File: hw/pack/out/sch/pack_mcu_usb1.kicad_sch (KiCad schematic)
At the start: 23 parts, among them J2 USB-C, J3 SWD, U1 BT40NE, U7 USBLC6-2SC6

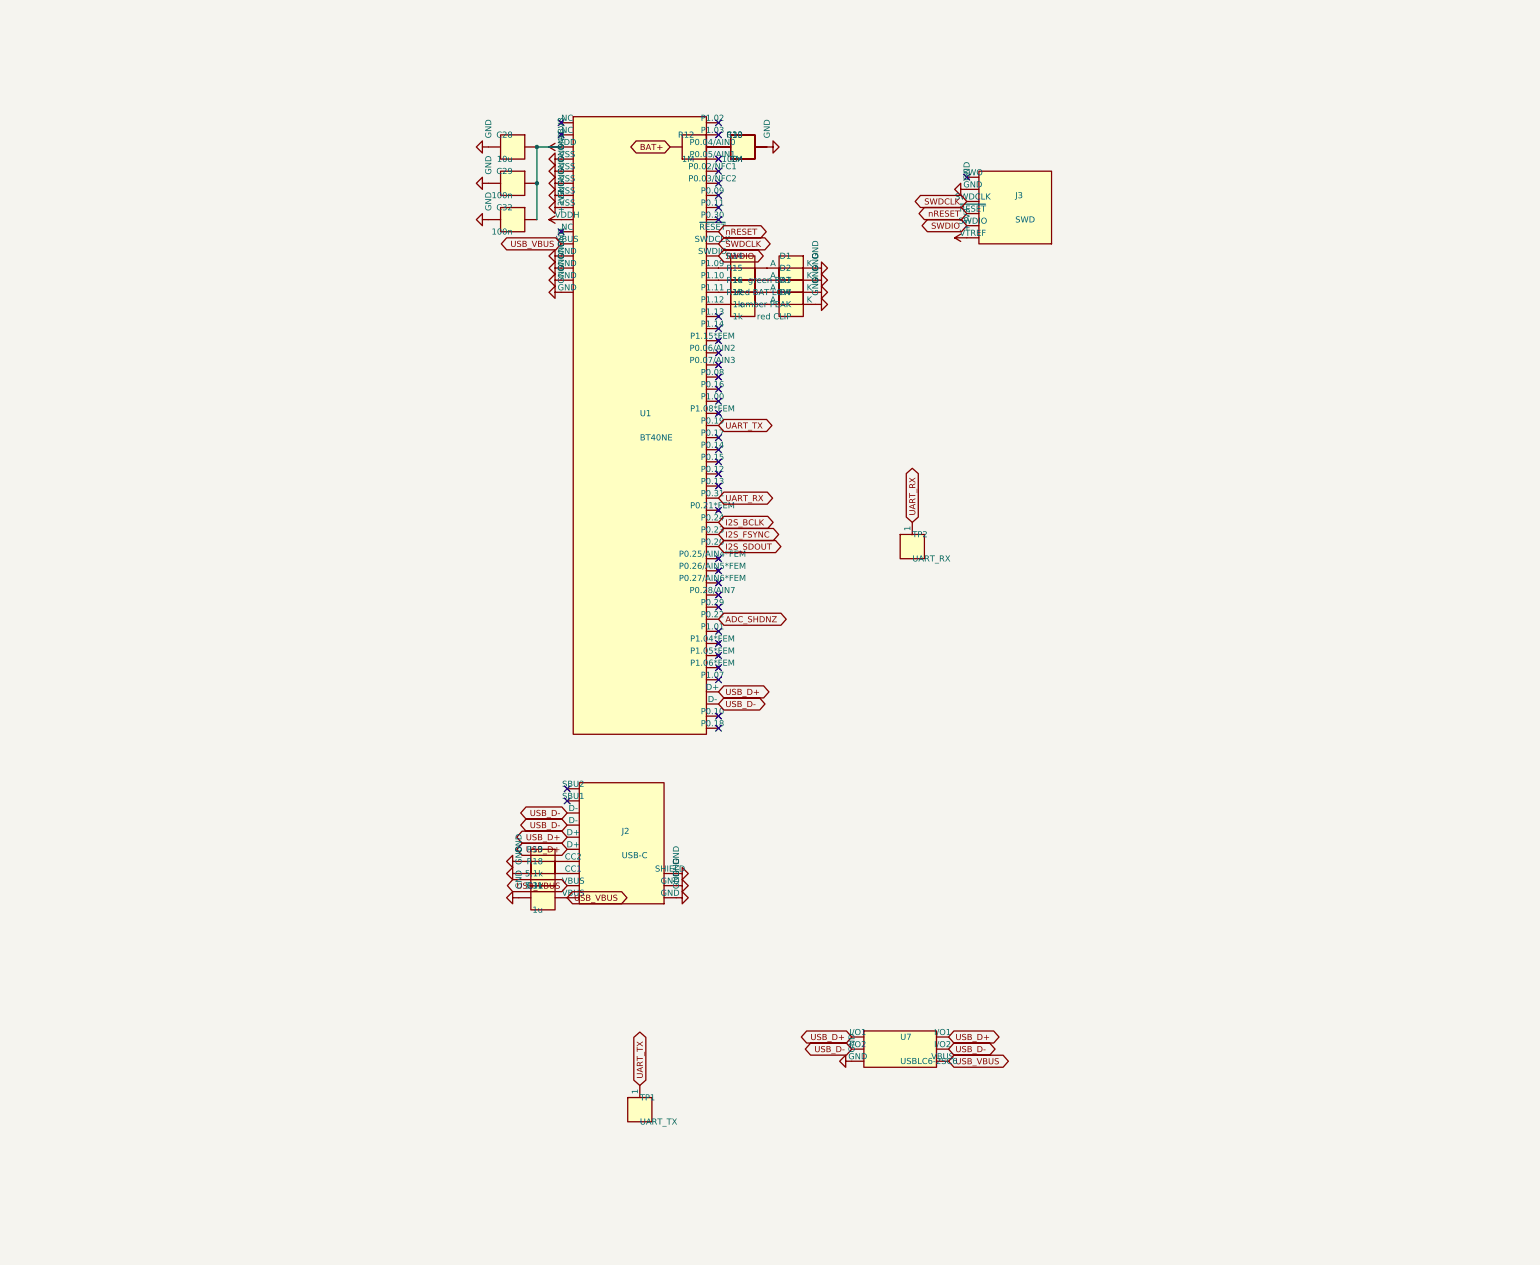
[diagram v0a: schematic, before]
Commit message: pack: #104 review fixes: 1 mm L1 battery path, test points, clip inserts off the antenna, pigtail route, JLC LCSC/rotations (#34)
- router: 'bat' class (1.0 mm, L1 only, necks <=1.36 mm at small pads);
  SW1 on-throw moved to pin 3 so feed and VSYS don't cross; 40 mOhm path
- audit.py: cell path from the board tracks (121 mOhm total, est. spring):
  cutoff computes 3.2012 V -> rounds to 3.3 V (reported, not tuned)
- TP3-TP11 folded in from review-104-tps (415194b), TP5/TP9-11 moved
- mech: clip inserts to (-24,3)/(-24,17) under the board; PIGTAIL route,
  bend radius, tie-down; fit.py checks both
- outputs: LCSC # per BOM line (verified), DNP/CONSIGN, CPL rotation table
- tests: battery path layer/width/R, BOM LCSC-or-DNP, rotation table

Co-Authored-By: Claude Opus 5.5 <noreply@anthropic.com>
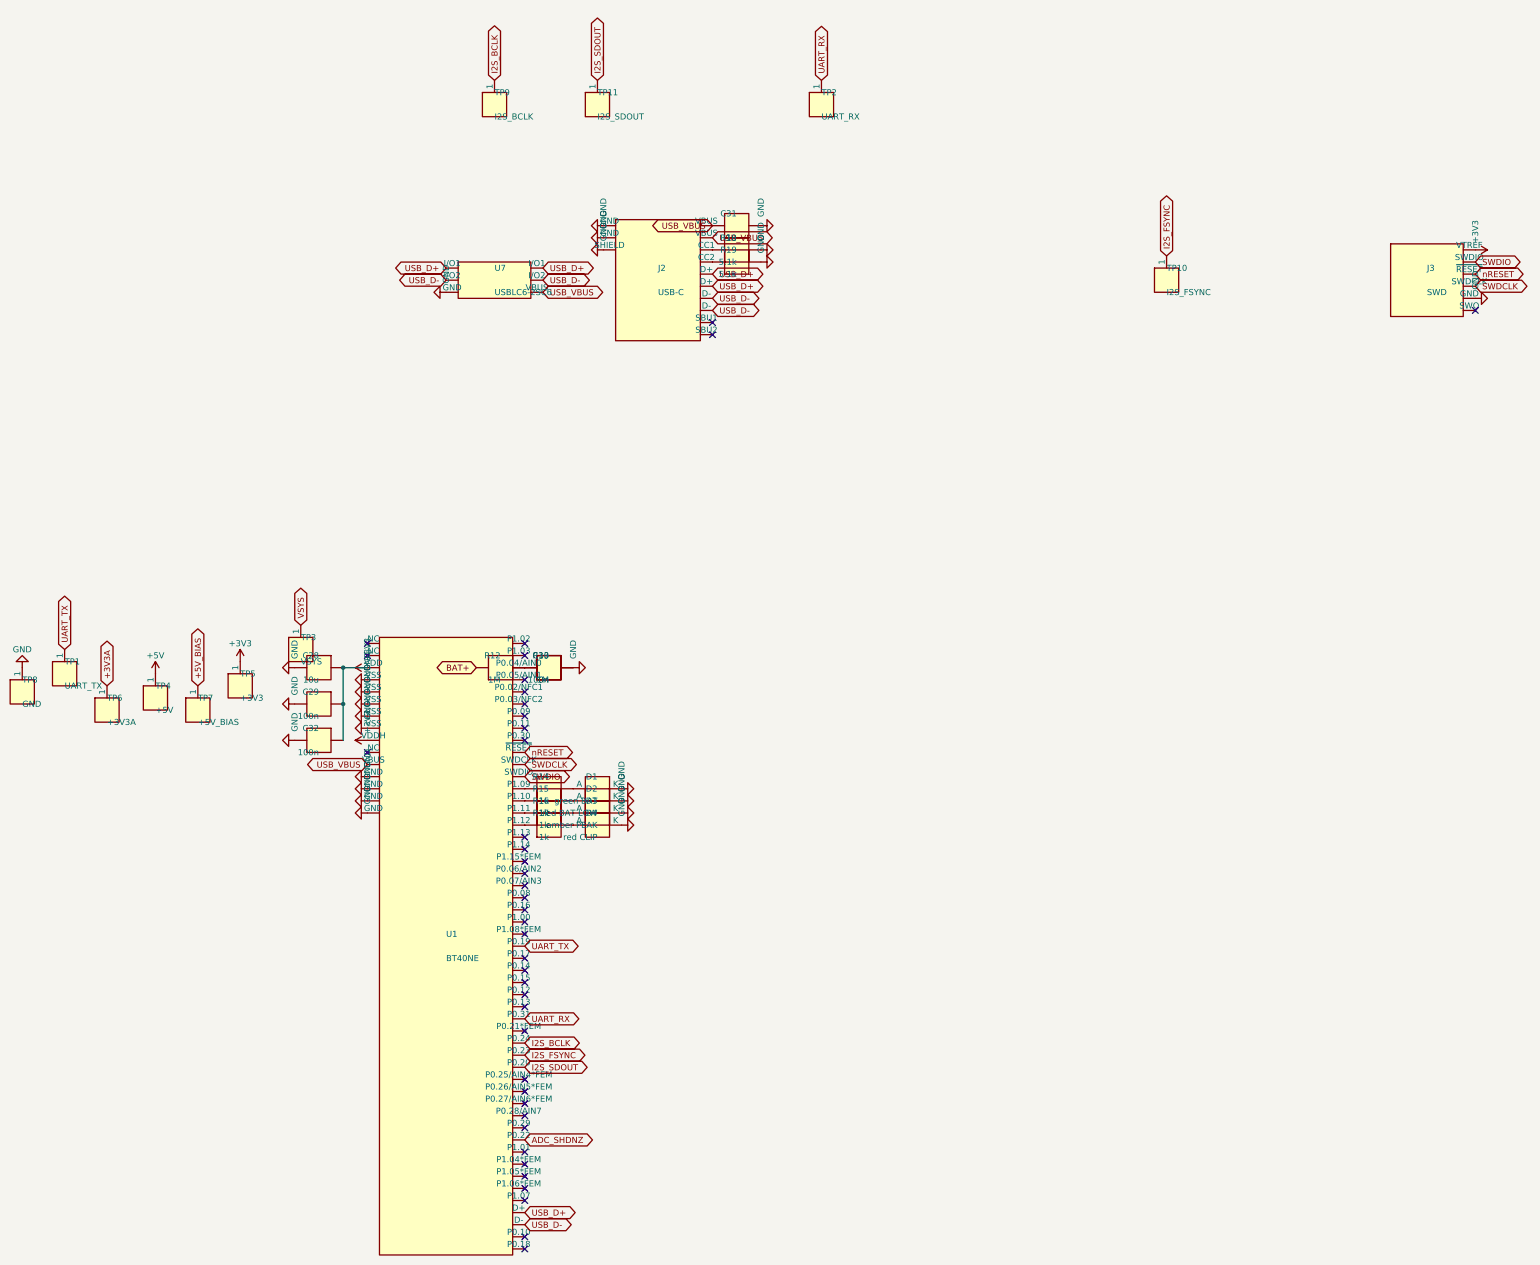
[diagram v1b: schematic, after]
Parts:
- added TP10: I2S_FSYNC, TestPoint:TestPoint_Pad_D1.0mm, symbol openpack:TestPoint
- added TP11: I2S_SDOUT, TestPoint:TestPoint_Pad_D1.0mm, symbol openpack:TestPoint
- added TP3: VSYS, TestPoint:TestPoint_Pad_D1.0mm, symbol openpack:TestPoint
- added TP4: +5V, TestPoint:TestPoint_Pad_D1.0mm, symbol openpack:TestPoint
- added TP5: +3V3, TestPoint:TestPoint_Pad_D1.0mm, symbol openpack:TestPoint
- added TP6: +3V3A, TestPoint:TestPoint_Pad_D1.0mm, symbol openpack:TestPoint
- added TP7: +5V_BIAS, TestPoint:TestPoint_Pad_D1.0mm, symbol openpack:TestPoint
- added TP8: GND, TestPoint:TestPoint_Pad_D1.0mm, symbol openpack:TestPoint
- added TP9: I2S_BCLK, TestPoint:TestPoint_Pad_D1.0mm, symbol openpack:TestPoint
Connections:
- net +3V3: now also TP5.1
- net GND: now also TP8.1
- net I2S_BCLK: now also TP9.1
- net I2S_FSYNC: now also TP10.1
- net I2S_SDOUT: now also TP11.1
- new net +3V3A: TP6.1
- new net +5V: TP4.1
- new net +5V_BIAS: TP7.1
- new net VSYS: TP3.1
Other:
- moved on the sheet: C28, C29, C30, C31, C32, D1, D2, D3, D4, J2, J3, R12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
